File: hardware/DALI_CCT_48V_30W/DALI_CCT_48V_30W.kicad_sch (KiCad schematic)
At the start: 86 parts, among them J1 Phoenix 5.08mm 2-pin 48V_IN, J2 DALI_A/DALI_B Phoenix 5.08mm, J3 LED+/WW-/CW- Phoenix 5.08mm, J4 SWD 1.27mm 4-pin (GND/SWDIO/S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, Q1 AON7534 N-ch 30V 25A, Q2 AON7534 N-ch 30V 25A, Q3 AON6424 N-ch 40V 20A, Q4 AON6424 N-ch 40V 20A

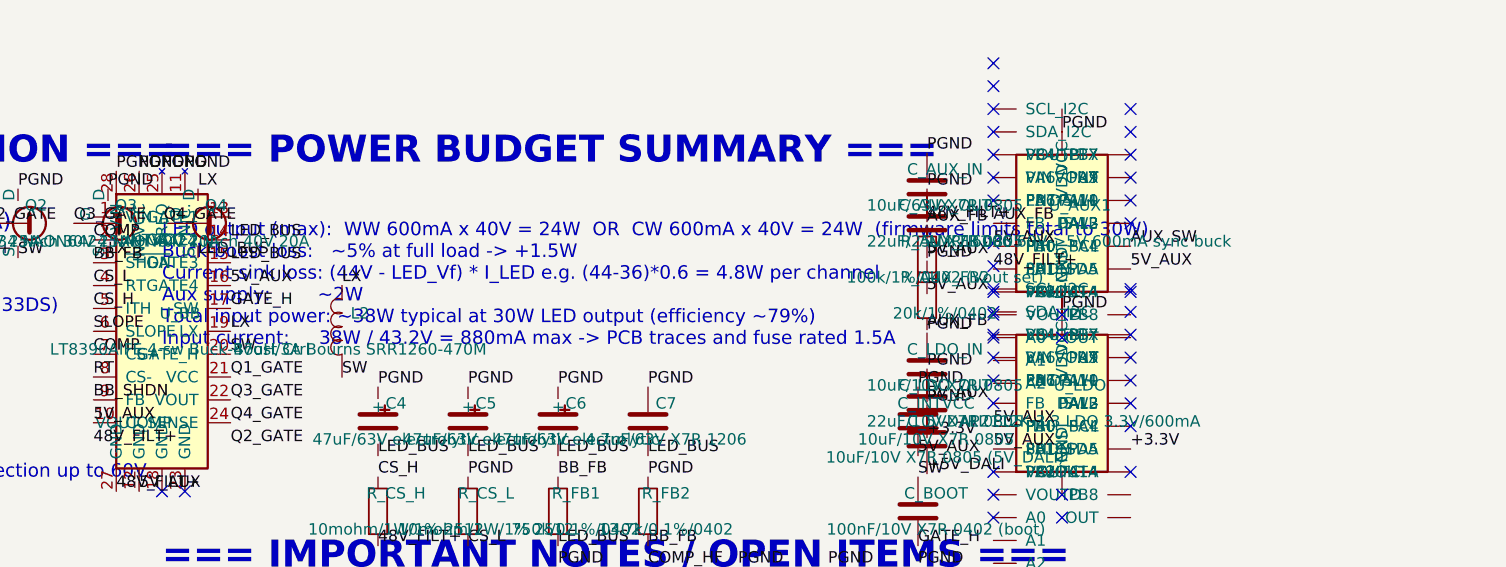
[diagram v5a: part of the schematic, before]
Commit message: fix: update power calculations and hardware max current to match 600mA operating point
Co-authored-by: manuelh83 <208121220+manuelh83@users.noreply.github.com>
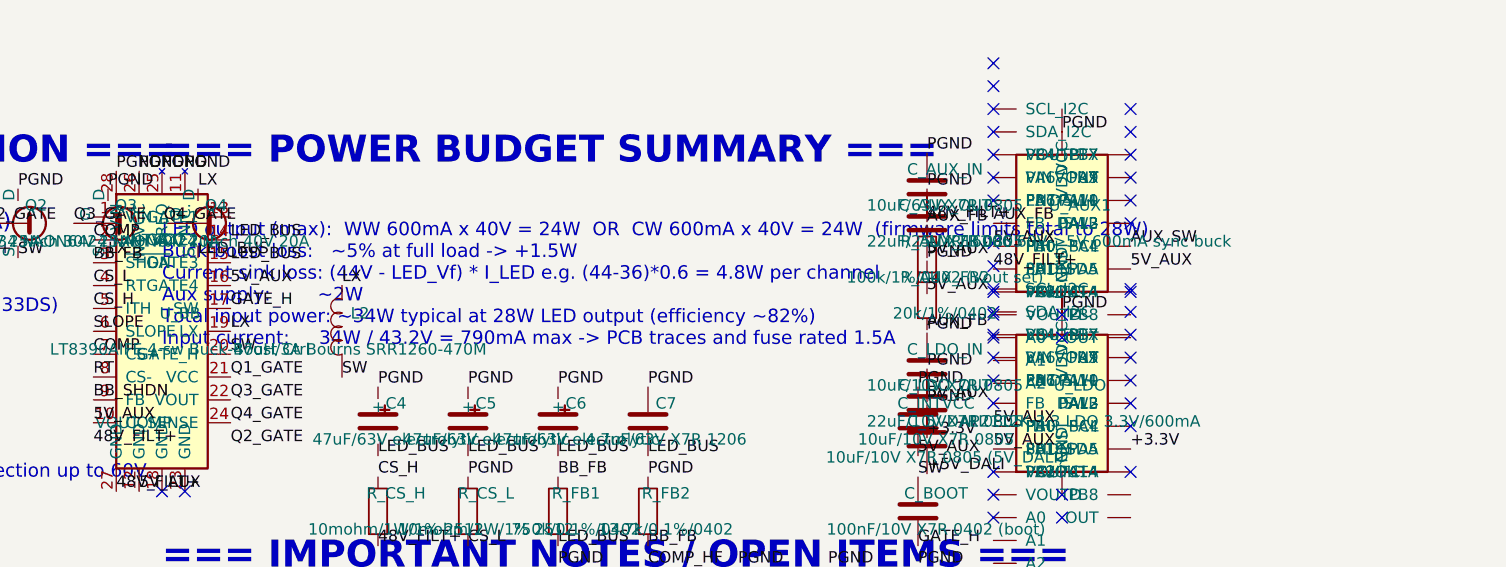
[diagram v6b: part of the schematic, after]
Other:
- note added: "LED output (max): WW 600mA x 40V = 24W OR CW 600mA x 40V = 24W (firmware limits total to 28W) Buck-boost loss: ~5% at full load -> +1.5W Current sink loss: (44V - LED_Vf) * I_LED e.g. (44-36)*0.6 = 4.8W per channel Aux supply: ~2W Total input power: ~34W typical at 28W LED output (efficiency ~82%) Input current: 34W / 43.2V = 790mA max -> PCB traces and fuse rated 1.5A"
- note removed: "LED output (max): WW 600mA x 40V = 24W OR CW 600mA x 40V = 24W (firmware limits total to 30W) Buck-boost loss: ~5% at full load -> +1.5W Current sink loss: (44V - LED_Vf) * I_LED e.g. (44-36)*0.6 = 4.8W per channel Aux supply: ~2W Total input power: ~38W typical at 30W LED output (efficiency ~79%) Input current: 38W / 43.2V = 880mA max -> PCB traces and fuse rated 1.5A"
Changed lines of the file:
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@@
     (effects (font (size 3 3) (bold yes)) (justify left))
   )
-  (text "LED output (max):  WW 600mA x 40V = 24W  OR  CW 600mA x 40V = 24W  (firmware limits total to 30W)\nBuck-boost loss:   ~5% at full load -> +1.5W\nCurrent sink loss: (44V - LED_Vf) * I_LED e.g. (44-36)*0.6 = 4.8W per channel\nAux supply:        ~2W\nTotal input power: ~38W typical at 30W LED output (efficiency ~79%)\nInput current:     38W / 43.2V = 880mA max -> PCB traces and fuse rated 1.5A"
+  (text "LED output (max):  WW 600mA x 40V = 24W  OR  CW 600mA x 40V = 24W  (firmware limits total to 28W)\nBuck-boost loss:   ~5% at full load -> +1.5W\nCurrent sink loss: (44V - LED_Vf) * I_LED e.g. (44-36)*0.6 = 4.8W per channel\nAux supply:        ~2W\nTotal input power: ~34W typical at 28W LED output (efficiency ~82%)\nInput current:     34W / 43.2V = 790mA max -> PCB traces and fuse rated 1.5A"
     (exclude_from_sim no)
     (at 120 38 0)
